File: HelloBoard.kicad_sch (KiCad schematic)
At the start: 36 parts, among them J1 USB_B_Micro, J2 Conn_01x04_Pin, J3 Conn_01x04_Pin, J4 Conn_02x08_Top_Bottom, SW1 SW_Push, SW2 SW_Push, U1 STM32F103C8T6, U2 AMS1117-3.3, U3 TMP235A2DCKR, U4 ADXL343, U5 DA56-11CGKWA, Y1 16MHz

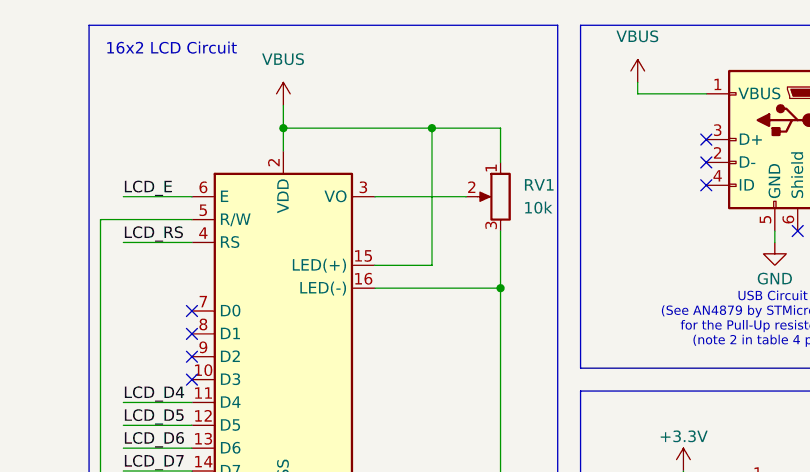
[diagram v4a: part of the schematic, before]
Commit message: Added footprints for layout
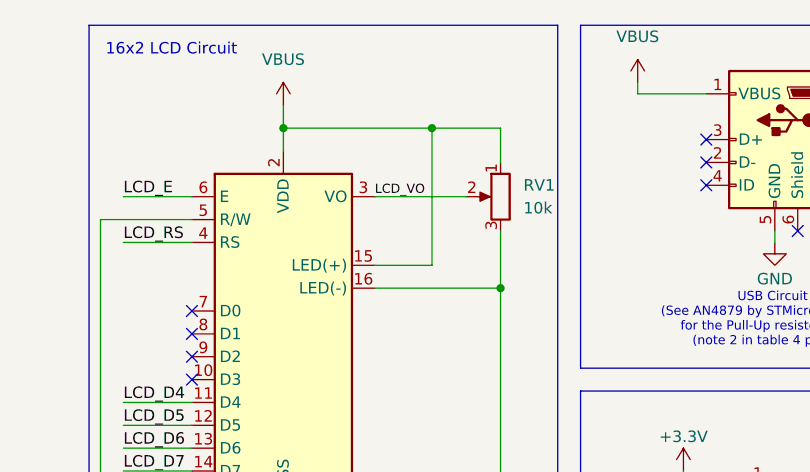
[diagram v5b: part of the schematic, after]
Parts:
- C1, C10, C11, C14, C2, C3, C4, C6, C7, C8, C9: footprint (none) -> Capacitor_SMD:C_0402_1005Metric
- C12: footprint (none) -> Capacitor_Tantalum_SMD:CP_EIA-3528-21_Kemet-B
- C13: footprint (none) -> Capacitor_Tantalum_SMD:CP_EIA-6032-15_Kemet-U
- C5: footprint (none) -> Capacitor_SMD:C_0603_1608Metric
- D1, D2: footprint (none) -> LED_SMD:LED_0201_0603Metric
- FB1: footprint (none) -> Inductor_SMD:L_0603_1608Metric
- J1: footprint (none) -> Connector_USB:USB_Micro-B_Wuerth_629105150521
- J2, J3: footprint (none) -> Connector_PinHeader_2.54mm:PinHeader_1x04_P2.54mm_Vertical
- J4: footprint Connector_PinHeader_1.00mm:PinHeader_2x08_P1.00mm_Vertical -> Connector_PinHeader_2.54mm:PinHeader_2x08_P2.54mm_Vertical
- R1, R2, R3, R4, R5: footprint (none) -> Resistor_SMD:R_0603_1608Metric
- RV1: footprint (none) -> Potentiometer_SMD:Potentiometer_Bourns_3214W_Vertical
- SW1, SW2: footprint (none) -> Button_Switch_THT:SW_PUSH_6mm_H5mm
- Y1: footprint (none) -> Crystal:Crystal_SMD_3225-4Pin_3.2x2.5mm
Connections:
- net LCD_VO: now reaches DS2.3 (VO), RV1.2
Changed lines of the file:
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@@
 	(title_block
 		(title "HelloBoard !")
-		(date "2026-03-05")
+		(date "2026-03-09")
 		(rev "1.0")
 		(company "University Of Jordan")
@@
 		)
 	)
+	(label "LCD_VO"
+		(at 219.71 31.75 0)
+		(effects
+			(font
+				(size 1.016 1.016)
+			)
+			(justify left bottom)
+		)
+	)
 	(label "LCD_RS"
 		(at 191.77 36.83 0)
@@
 			)
 		)
-		(property "Footprint" ""
+		(property "Footprint" "Connector_PinHeader_2.54mm:PinHeader_1x04_P2.54mm_Vertical"
 			(at 265.43 66.04 0)
 			(effects
@@
 			)
 		)
-		(property "Footprint" ""
+		(property "Footprint" "Resistor_SMD:R_0603_1608Metric"
 			(at 108.458 184.15 90)
 			(effects
@@
 			)
 		)
-		(property "Footprint" ""
+		(property "Footprint" "Capacitor_SMD:C_0402_1005Metric"
 			(at 25.0952 114.3 0)
 			(effects
@@
 			)
 		)
-		(property "Footprint" ""
+		(property "Footprint" "Button_Switch_THT:SW_PUSH_6mm_H5mm"
 			(at 22.86 30.48 0)
 			(effects
@@
 			)
 		)
-		(property "Footprint" ""
+		(property "Footprint" "Capacitor_SMD:C_0402_1005Metric"
 			(at 110.1852 31.75 0)
 			(effects
@@
 			)
 		)
-		(property "Footprint" ""
+		(property "Footprint" "Capacitor_SMD:C_0402_1005Metric"
 			(at 87.3252 31.75 0)
 			(effects
@@
 			)
 		)
-		(property "Footprint" ""
+		(property "Footprint" "Capacitor_SMD:C_0402_1005Metric"
 			(at 40.3352 33.02 0)
 			(effects
@@
 			)
 		)
-		(property "Footprint" ""
+		(property "Footprint" "Capacitor_SMD:C_0402_1005Metric"
 			(at 144.4752 36.83 0)
 			(effects
@@
 			)
 		)
-		(property "Footprint" ""
+		(property "Footprint" "Capacitor_SMD:C_0402_1005Metric"
 			(at 234.6452 105.41 0)
 			(effects
@@
 			)
 		)
-		(property "Footprint" ""
+		(property "Footprint" "Connector_PinHeader_2.54mm:PinHeader_1x04_P2.54mm_Vertical"
 			(at 15.24 179.07 0)
 			(effects
@@
 			)
 		)
-		(property "Footprint" ""
+		(property "Footprint" "Crystal:Crystal_SMD_3225-4Pin_3.2x2.5mm"
 			(at 35.56 106.68 0)
 			(effects
@@
 			)
 		)
-		(property "Footprint" ""
+		(property "Footprint" "Button_Switch_THT:SW_PUSH_6mm_H5mm"
 			(at 130.81 180.34 0)
 			(effects
@@
 			)
 		)
-		(property "Footprint" ""
+		(property "Footprint" "Connector_USB:USB_Micro-B_Wuerth_629105150521"
 			(at 260.35 26.67 0)
 			(effects
@@
 			)
 		)
-		(property "Footprint" ""
+		(property "Footprint" "Resistor_SMD:R_0603_1608Metric"
 			(at 46.99 66.548 90)
 			(effects
@@
 			)
 		)
-		(property "Footprint" ""
+		(property "Footprint" "Capacitor_SMD:C_0402_1005Metric"
 			(at 131.7752 36.83 0)
 			(effects
@@
 			)
 		)
-		(property "Footprint" ""
+		(property "Footprint" "Resistor_SMD:R_0603_1608Metric"
 			(at 26.162 175.26 90)
 			(effects
@@
 			)
 		)
-		(property "Footprint" ""
+		(property "Footprint" "Capacitor_SMD:C_0402_1005Metric"
 			(at 98.7552 31.75 0)
 			(effects
@@
 			)
 		)
-		(property "Footprint" "Connector_PinHeader_1.00mm:PinHeader_2x08_P1.00mm_Vertical"
+		(property "Footprint" "Connector_PinHeader_2.54mm:PinHeader_2x08_P2.54mm_Vertical"
 			(at 193.04 101.6 0)
 			(effects
@@
 			)
 		)
-		(property "Footprint" ""
+		(property "Footprint" "Capacitor_Tantalum_SMD:CP_EIA-6032-15_Kemet-U"
 			(at 42.8752 146.05 0)
 			(effects
@@
 			)
 		)
-		(property "Footprint" ""
+		(property "Footprint" "Resistor_SMD:R_0603_1608Metric"
 			(at 49.022 175.26 90)
 			(effects
@@
 			)
 		)
-		(property "Footprint" ""
+		(property "Footprint" "Potentiometer_SMD:Potentiometer_Bourns_3214W_Vertical"
 			(at 233.68 31.75 0)
 			(effects
@@
 			)
 		)
-		(property "Footprint" ""
+		(property "Footprint" "LED_SMD:LED_0201_0603Metric"
 			(at 99.06 179.07 0)
 			(effects
@@
 			)
 		)
-		(property "Footprint" ""
+		(property "Footprint" "Resistor_SMD:R_0603_1608Metric"
 			(at 62.738 142.24 90)
 			(effects
@@
 			)
 		)
-		(property "Footprint" ""
+		(property "Footprint" "Capacitor_SMD:C_0402_1005Metric"
 			(at 162.2552 36.83 0)
 			(effects
@@
 			)
 		)
-		(property "Footprint" ""
+		(property "Footprint" "Capacitor_SMD:C_0402_1005Metric"
 			(at 47.9552 114.3 0)
 			(effects
@@
 			)
 		)
-		(property "Footprint" ""
+		(property "Footprint" "Capacitor_SMD:C_0603_1608Metric"
 			(at 64.4652 31.75 0)
 			(effects
@@
 			)
 		)
-		(property "Footprint" ""
+		(property "Footprint" "LED_SMD:LED_0201_0603Metric"
 			(at 53.34 137.16 0)
 			(effects
@@
 			)
 		)
-		(property "Footprint" ""
+		(property "Footprint" "Capacitor_SMD:C_0402_1005Metric"
 			(at 75.8952 31.75 0)
 			(effects
@@
 			)
 		)
-		(property "Footprint" ""
+		(property "Footprint" "Capacitor_Tantalum_SMD:CP_EIA-3528-21_Kemet-B"
 			(at 17.4752 144.78 0)
 			(effects
@@
 			)
 		)
-		(property "Footprint" ""
+		(property "Footprint" "Inductor_SMD:L_0603_1608Metric"
 			(at 153.67 30.988 90)
 			(effects

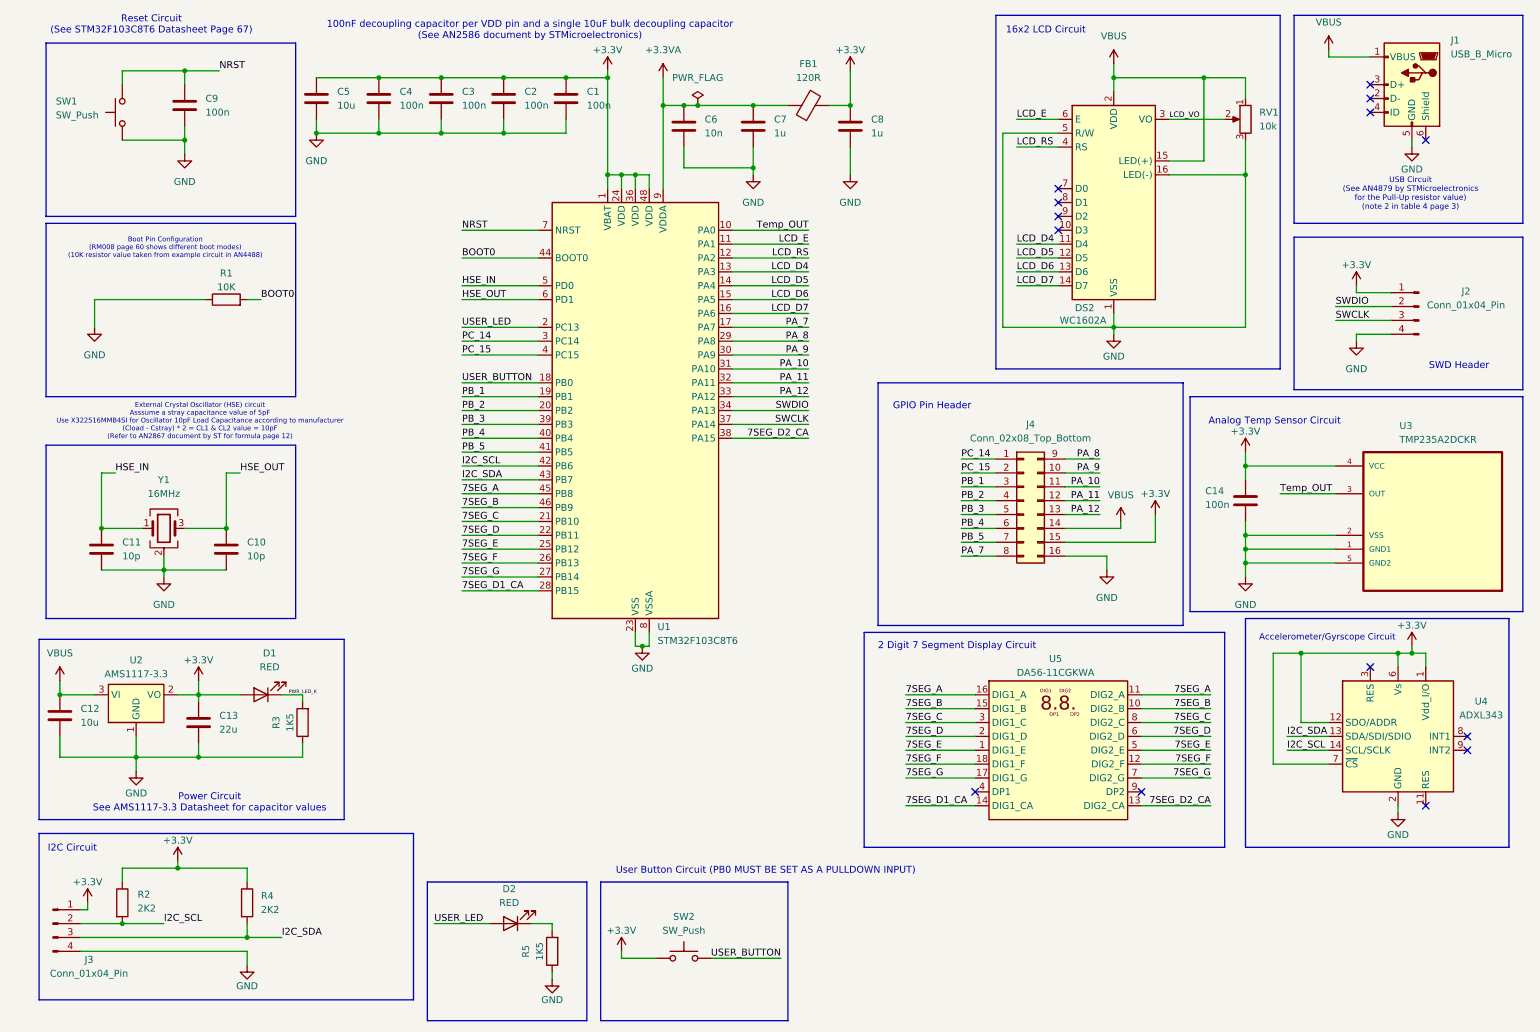
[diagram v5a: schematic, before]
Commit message: added SilkScreen images and external pulldown for user button
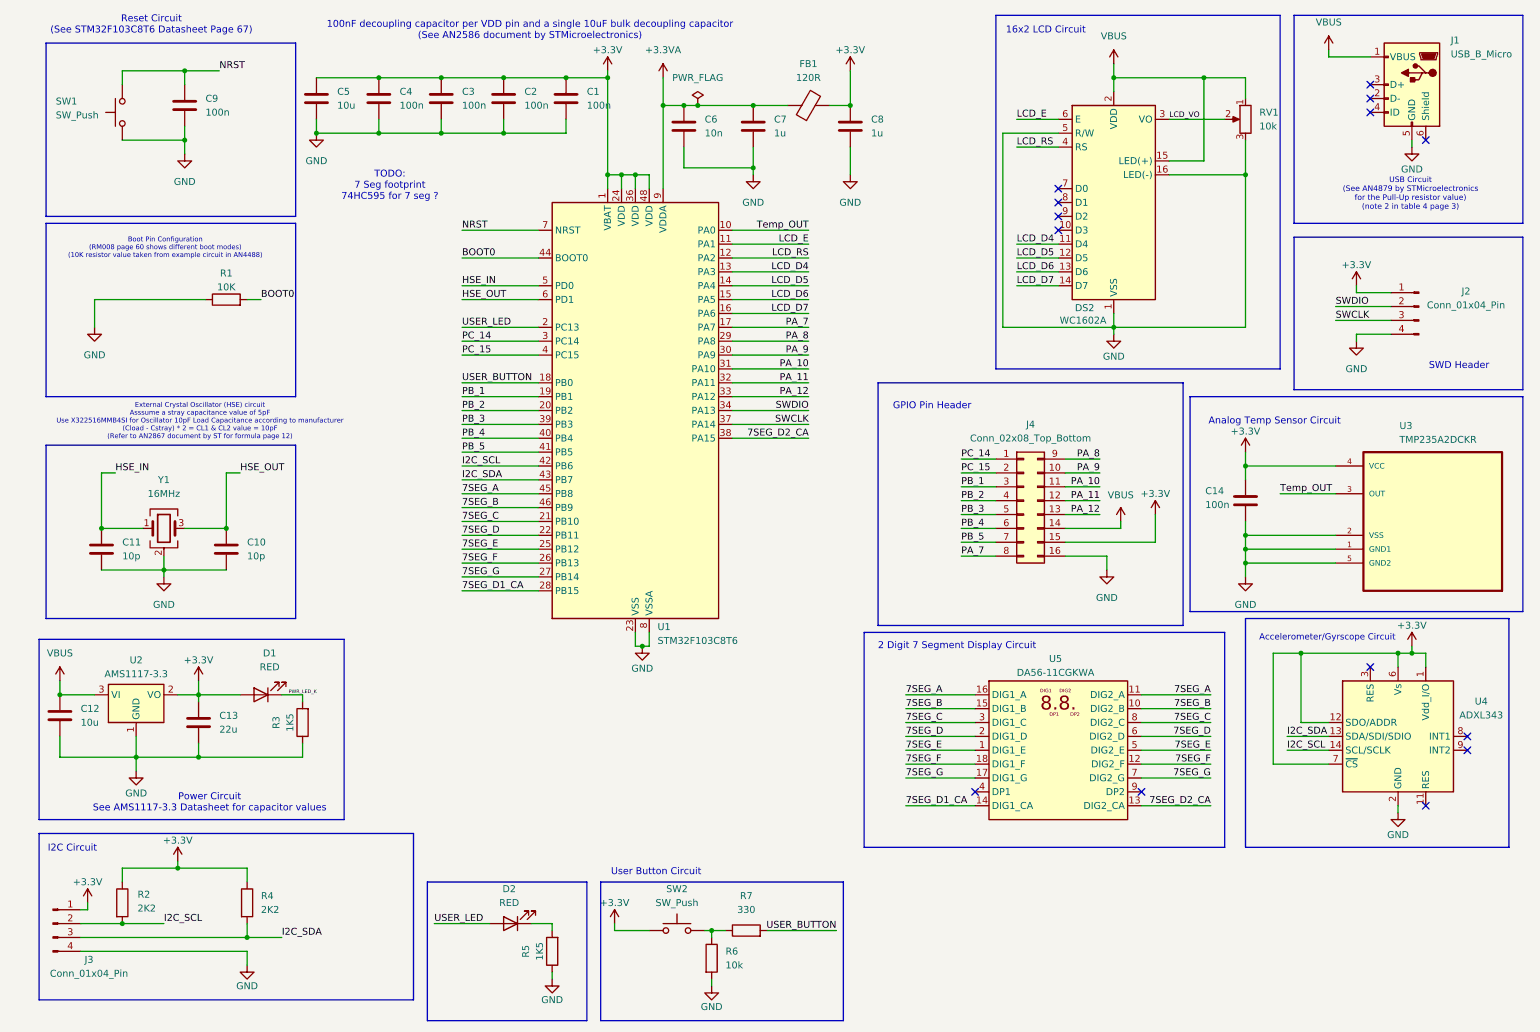
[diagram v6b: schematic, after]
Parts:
- added R6: 10k, Resistor_SMD:R_0603_1608Metric, symbol Device:R
- added R7: 330, Resistor_SMD:R_0402_1005Metric, symbol Device:R
- RV1: footprint Potentiometer_SMD:Potentiometer_Bourns_3214W_Vertical -> Potentiometer_THT:Potentiometer_Bourns_3296W_Vertical
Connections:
- net GND: now also R6.2
- net USER_BUTTON: now also R7.2; no longer SW2.2
- new net: R6.1, R7.1, SW2.2
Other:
- note added: "TODO: 7 Seg footprint 74HC595 for 7 seg ?"
- note added: "User Button Circuit"
- note removed: "User Button Circuit (PB0 MUST BE SET AS A PULLDOWN INPUT)"
- moved on the sheet: SW2

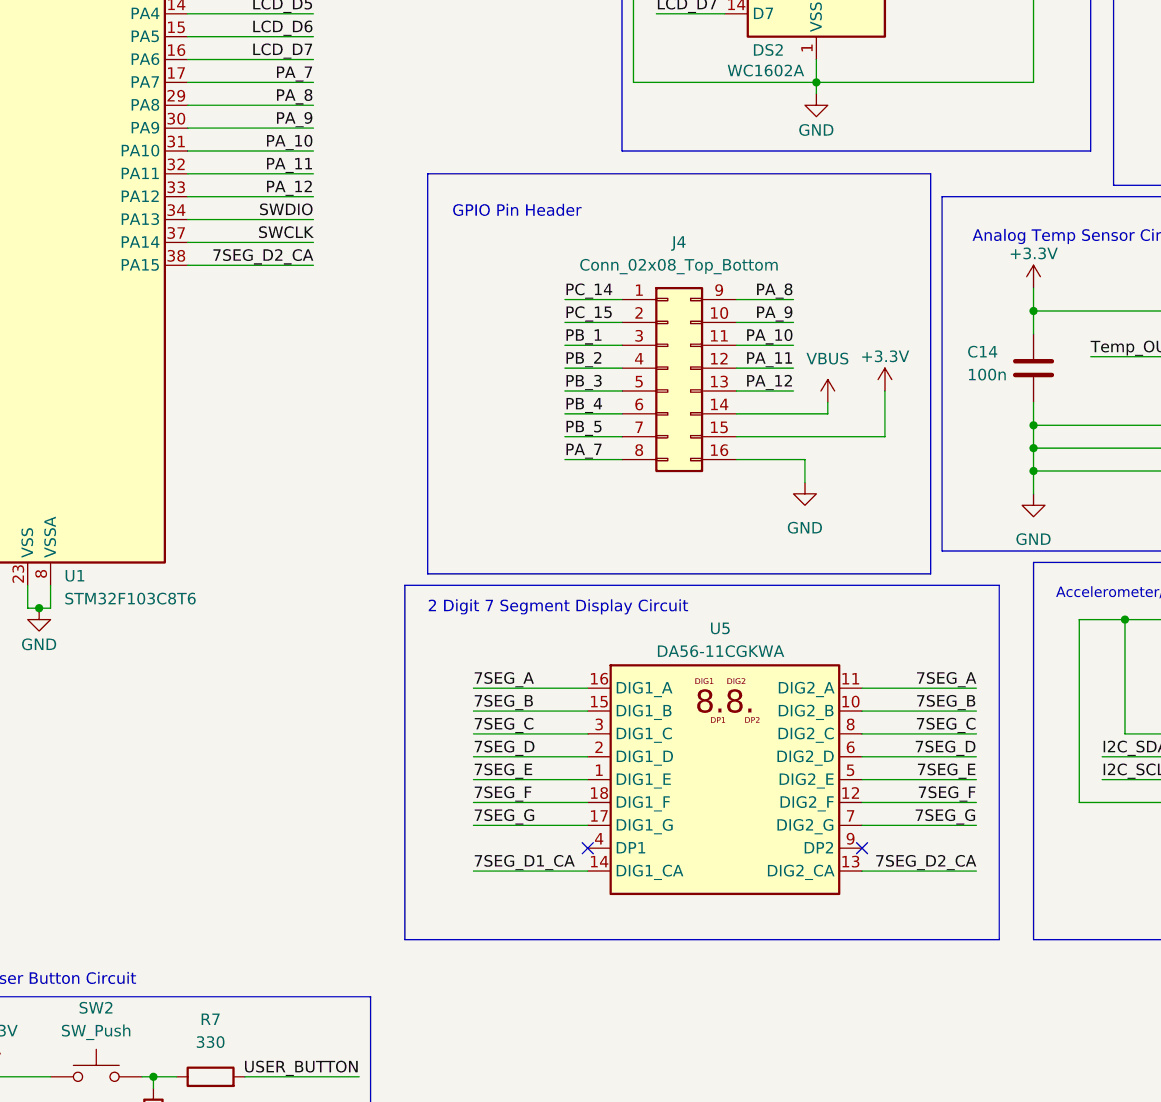
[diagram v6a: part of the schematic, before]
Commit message: swapped 7Seg footprint
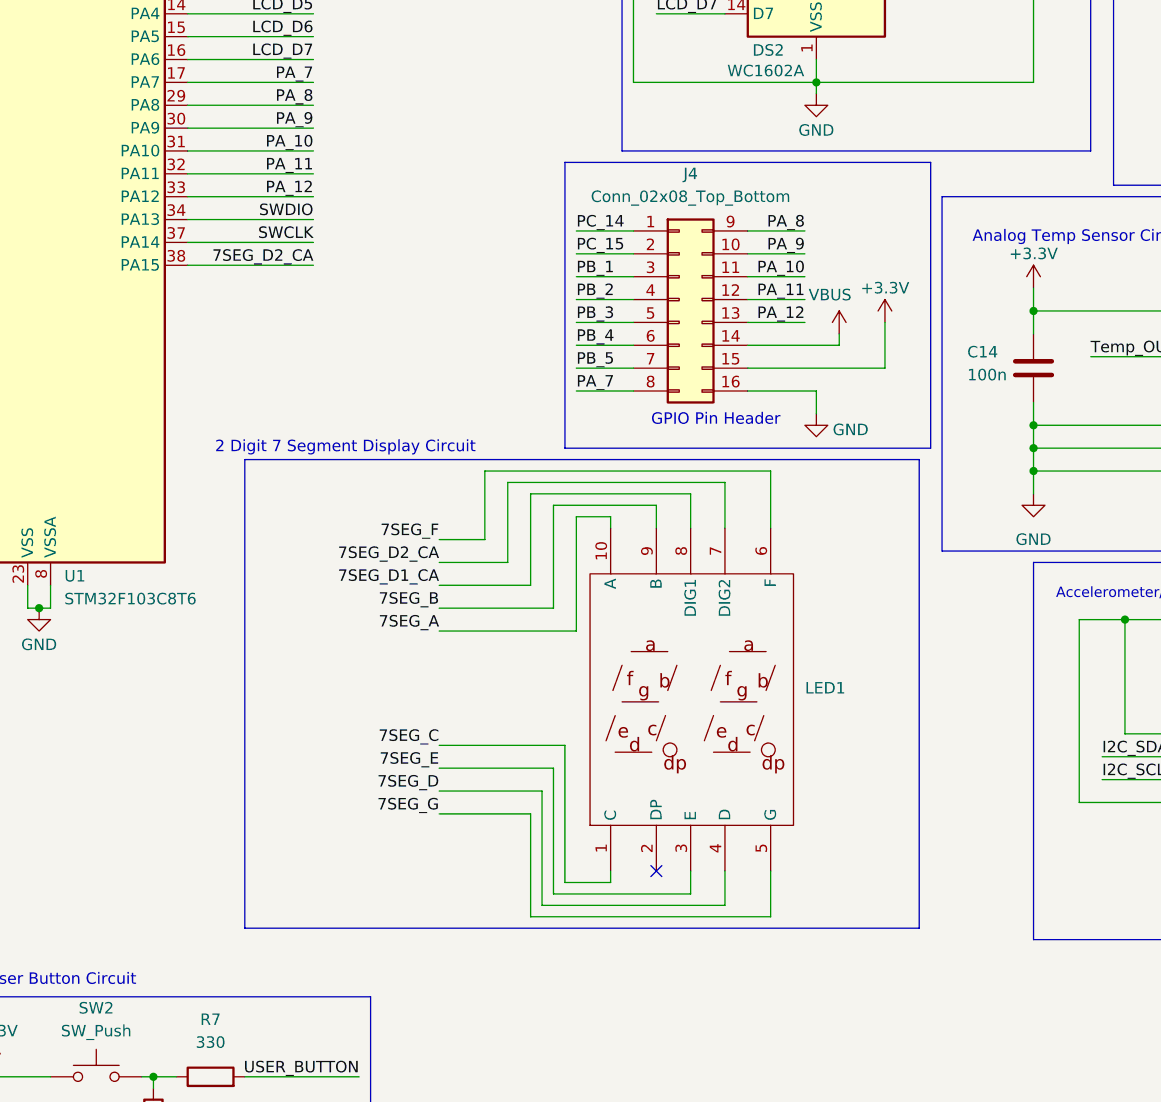
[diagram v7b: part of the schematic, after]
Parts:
- removed U5: DA56-11CGKWA, Display_7Segment:DA56-11CGKWA, symbol Display_Character:DA56-11CGKWA
- added LED1: ~, 7Segment2Digit:7Segment2Digit, symbol 7Segment2Digit:SN460561N/0.56Inch/ /2Bit
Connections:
- net 7SEG_A: now also LED1.10 (A)
- net 7SEG_B: now also LED1.9 (B)
- net 7SEG_C: now also LED1.1 (C)
- net 7SEG_D: now also LED1.4 (D)
- net 7SEG_D1_CA: now also LED1.8 (DIG1)
- net 7SEG_D2_CA: now also LED1.7 (DIG2)
- net 7SEG_E: now also LED1.3 (E)
- net 7SEG_F: now also LED1.6 (F)
- net 7SEG_G: now also LED1.5 (G)
- no-connect marks 14 -> 13
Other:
- moved on the sheet: J4

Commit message: started rough layout
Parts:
- added H1, H2, H3, H4: MountingHole, MountingHole:MountingHole_2.2mm_M2, symbol Mechanical:MountingHole
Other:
- note added: "7 Segment Display Circuit"
- note added: "Mounting Holes"
- note removed: "2 Digit 7 Segment Display Circuit"
